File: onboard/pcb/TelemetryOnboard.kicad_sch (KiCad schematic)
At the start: 140 parts, among them J1 USB-C, J2 USB-C, J3 RFPC-SMA28-F, J4 RFPC-SMA28-F, M1 M4 Mounting Hole, M2 M4 Mounting Hole, M3 M4 Mounting Hole, M4 M4 Mounting Hole, Q1 NPN, U1 CP2102N, U2 CP2102N, U3 RC1780HP-RC232, U4 RC1701HP-RC232, U5 AVR128DB64x-xPT, U6 W25Q80DVSSIG

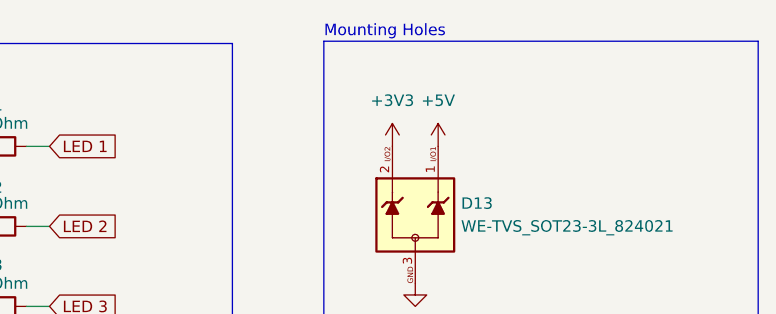
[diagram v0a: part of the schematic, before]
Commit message: change esd prot name
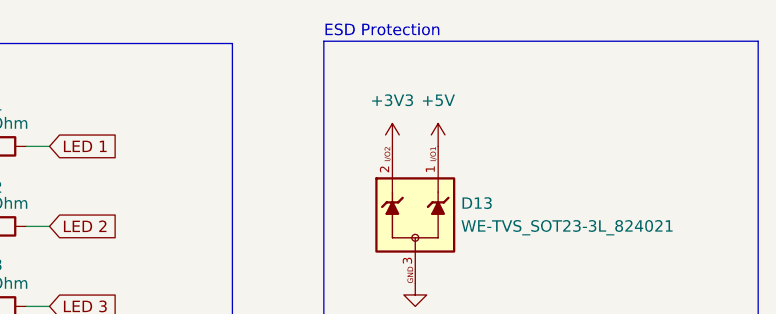
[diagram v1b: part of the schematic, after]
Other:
- note added: "ESD Protection"
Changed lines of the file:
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@@
 		)
 	)
-	(text "Mounting Holes"
+	(text "ESD Protection"
 		(exclude_from_sim no)
 		(at 520.7 24.13 0)

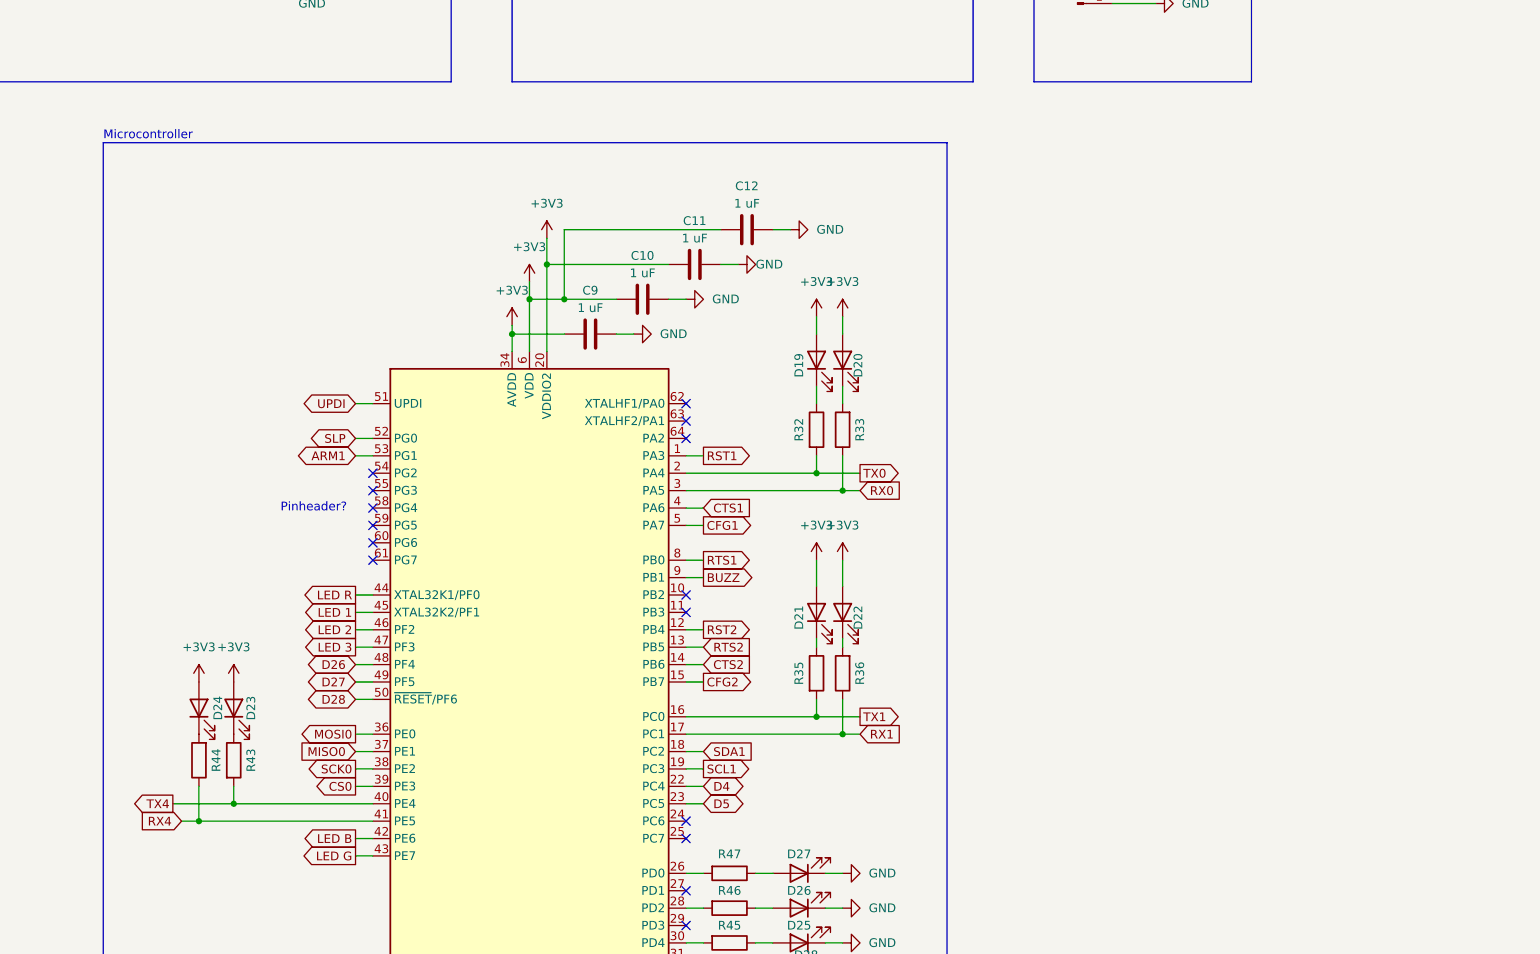
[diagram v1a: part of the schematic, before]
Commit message: add connector to umbilical connector
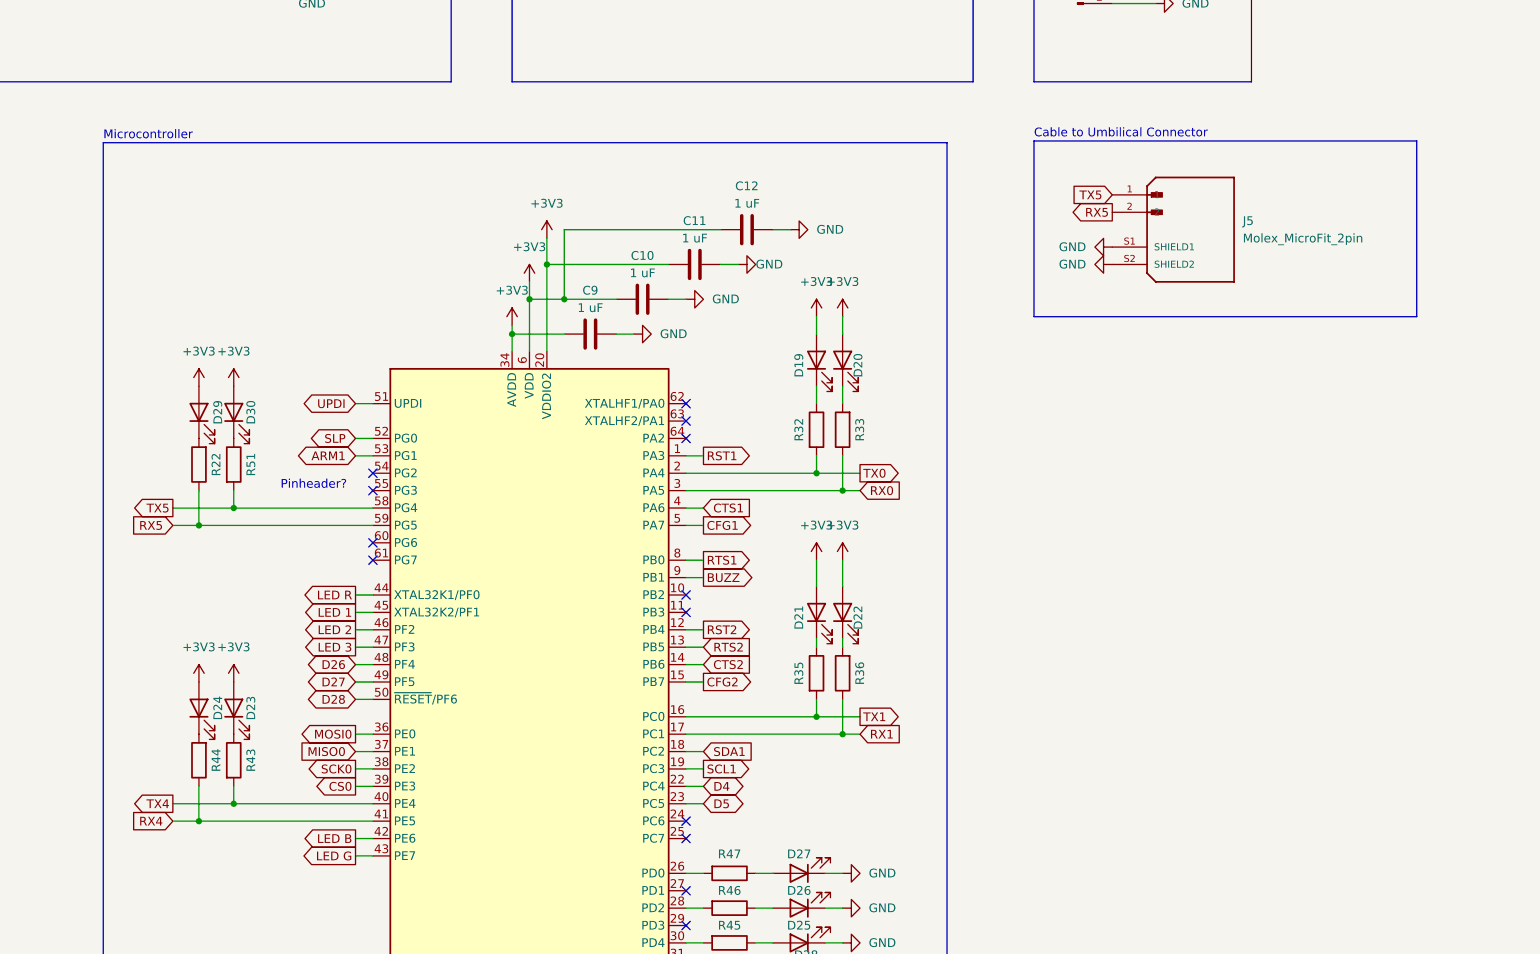
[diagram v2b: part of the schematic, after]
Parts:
- added D29, D30: red, LED_SMD:LED_0805_2012Metric_Pad1.15x1.40mm_HandSolder, symbol Device:LED
- added J5: Molex_MicroFit_2pin, Footprints:Molex_MicroFit_2pin, symbol Symbols:Molex_MicroFit_2pin
- added R22, R51: 1k, Resistor_SMD:R_0805_2012Metric_Pad1.20x1.40mm_HandSolder, symbol Device:R
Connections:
- net +3V3: now also D29.2 (A), D30.2 (A)
- net GND: now also J5.S1 (SHIELD1), J5.S2 (SHIELD2)
- net TX5: now reaches U5.58 (PG4)
- net TX5: now also J5.1, R51.2
- net RX5: now reaches U5.59 (PG5)
- net RX5: now also J5.2, R22.1
- new net: D29.1 (K), R22.2
- new net: D30.1 (K), R51.1
- no-connect marks 41 -> 39
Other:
- note added: "Cable to Umbilical Connector"

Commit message: place other components on pcb
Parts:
- removed D29, D30: red, LED_SMD:LED_0805_2012Metric_Pad1.15x1.40mm_HandSolder, symbol Device:LED
- removed R22, R51: 1k, Resistor_SMD:R_0805_2012Metric_Pad1.20x1.40mm_HandSolder, symbol Device:R
- removed TP9: TestPoint, Footprints:Test Point, symbol Connector:TestPoint
- added D21, D22: red, LED_SMD:LED_0805_2012Metric_Pad1.15x1.40mm_HandSolder, symbol Device:LED
- added R35, R36: 1k, Resistor_SMD:R_0805_2012Metric_Pad1.20x1.40mm_HandSolder, symbol Device:R
- TP36, TP37, TP38, TP39: now not fitted
- renumbered D21 to D29, D22 to D30, R35 to R22, R36 to R51
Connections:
- net +3V3: now also D21.2 (A), D22.2 (A)
- net BUZZ: now also U5.8 (PB0); no longer U5.9 (PB1)
- net CFG1: now also U5.3 (PA5); no longer U5.5 (PA7)
- net CFG2: now also U5.11 (PB3); no longer U5.15 (PB7)
- net CTS1: now also TP8.1, U5.1 (PA3); no longer TP4.1, U5.4 (PA6)
- net CTS2: now also TP13.1, U5.9 (PB1); no longer TP14.1, U5.14 (PB6)
- net D4: now also U5.24 (PC6); no longer U5.22 (PC4)
- net D5: now also U5.25 (PC7); no longer U5.23 (PC5)
- net LED 1: now also U5.47 (PF3); no longer U5.45 (XTAL32K2/PF1)
- net LED 3: now also U5.45 (XTAL32K2/PF1); no longer U5.47 (PF3)
- net RST1: now also U5.61 (PG7); no longer U5.1 (PA3)
- net RST2: now also U5.60 (PG6); no longer U5.12 (PB4)
- net RTS1: now also TP4.1, U5.2 (PA4); no longer TP8.1, U5.8 (PB0)
- net RTS2: now also TP14.1, U5.10 (PB2); no longer TP13.1, U5.13 (PB5)
- net RX0: now also U5.63 (XTALHF2/PA1); no longer U5.3 (PA5)
- net RX1: now also J5.1; no longer TP17.1, U4.5 (TXD)
- net TX0: now also U5.62 (XTALHF1/PA0); no longer U5.2 (PA4)
- net TX1: now also J5.2; no longer R37.1, TP16.1, U4.6 (RXD)
- net at R47.2: now also U5.15 (PB7); no longer U5.26 (PD0)
- net at R46.2: now also U5.14 (PB6); no longer U5.28 (PD2)
- net RX5: no longer names the net of U5.59 (PG5)
- net RX5: no longer J5.2
- net TX5: no longer names the net of U5.58 (PG4)
- net TX5: no longer J5.1
- new net: D22.1 (K), R36.2
- new net: D21.1 (K), R35.1
- new net RX3: R36.1, TP17.1, U4.5 (TXD), U5.13 (PB5)
- new net TX3: R35.2, R37.1, TP16.1, U4.6 (RXD), U5.12 (PB4)
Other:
- moved on the sheet: D19, D20, D26, D27, D29, D30, J5, R22, R32, R33, R46, R47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

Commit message: improve pcb layout
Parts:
- removed D23, D24: red, LED_SMD:LED_0805_2012Metric_Pad1.15x1.40mm_HandSolder, symbol Device:LED
- removed D28: orange, LED_SMD:LED_0805_2012Metric_Pad1.15x1.40mm_HandSolder, symbol Device:LED
- removed R43, R44: 1k, Resistor_SMD:R_0805_2012Metric_Pad1.20x1.40mm_HandSolder, symbol Device:R
- removed R48: 270R, Resistor_SMD:R_0805_2012Metric_Pad1.20x1.40mm_HandSolder, symbol Device:R
- renumbered D26 to D25, D27 to D26, D25 to D27, R46 to R45, R47 to R46, R45 to R47
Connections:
- net at U5.30 (PD4): no longer R47.2
- net at U5.33 (VREFA/PD7): now also R47.2
- no-connect marks 39 -> 40
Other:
- moved on the sheet: D27, R47

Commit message: small change
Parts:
- D11, D12, R20, R21: now fitted
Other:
- moved on the sheet: J5
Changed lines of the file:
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@@
 	)
 	(rectangle
-		(start 509.27 141.986)
-		(end 565.15 167.64)
+		(start 497.84 143.256)
+		(end 553.72 168.91)
 		(stroke
 			(width 0)
@@
 	(text "Cable to Umbilical Connector"
 		(exclude_from_sim no)
-		(at 509.27 140.97 0)
+		(at 497.84 142.24 0)
 		(effects
 			(font
@@
 	(global_label "TX1"
 		(shape input)
-		(at 520.7 152.4 180)
+		(at 509.27 153.67 180)
 		(fields_autoplaced yes)
 		(effects
@@
 		)
 		(property "Intersheetrefs" "${INTERSHEET_REFS}"
-			(at 514.3282 152.4 0)
+			(at 502.8982 153.67 0)
 			(effects
 				(font
@@
 	(global_label "RX1"
 		(shape output)
-		(at 520.7 149.86 180)
+		(at 509.27 151.13 180)
 		(fields_autoplaced yes)
 		(effects
@@
 		)
 		(property "Intersheetrefs" "${INTERSHEET_REFS}"
-			(at 514.0258 149.86 0)
+			(at 502.5958 151.13 0)
 			(effects
 				(font
@@
 	(symbol
 		(lib_id "power:GND")
-		(at 520.7 157.48 270)
+		(at 509.27 158.75 270)
 		(unit 1)
 		(exclude_from_sim no)
@@
 		(fields_autoplaced yes)
 		(property "Reference" "#PWR0111"
-			(at 514.35 157.48 0)
+			(at 502.92 158.75 0)
 			(effects
 				(font
@@
 		)
 		(property "Value" "GND"
-			(at 516.89 157.4799 90)
+			(at 505.46 158.7499 90)
 			(effects
 				(font
@@
 		)
 		(property "Footprint" ""
-			(at 520.7 157.48 0)
+			(at 509.27 158.75 0)
 			(effects
 				(font
@@
 		)
 		(property "Datasheet" ""
-			(at 520.7 157.48 0)
+			(at 509.27 158.75 0)
 			(effects
 				(font
@@
 		)
 		(property "Description" "Power symbol creates a global label with name \"GND\" , ground"
-			(at 520.7 157.48 0)
+			(at 509.27 158.75 0)
 			(effects
 				(font
@@
 	(symbol
 		(lib_id "Symbols:Molex_MicroFit_2pin")
-		(at 525.78 154.94 0)
+		(at 514.35 156.21 0)
 		(unit 1)
 		(exclude_from_sim no)
@@
 		(fields_autoplaced yes)
 		(property "Reference" "J5"
-			(at 539.75 153.6699 0)
+			(at 528.32 154.9399 0)
 			(effects
 				(font
@@
 		)
 		(property "Value" "Molex_MicroFit_2pin"
-			(at 539.75 156.2099 0)
+			(at 528.32 157.4799 0)
 			(effects
 				(font
@@
 		)
 		(property "Footprint" "Footprints:Molex_MicroFit_2pin"
-			(at 525.78 154.94 0)
+			(at 514.35 156.21 0)
 			(effects
 				(font
@@
 		)
 		(property "Datasheet" ""
-			(at 525.78 154.94 0)
+			(at 514.35 156.21 0)
 			(effects
 				(font
@@
 		)
 		(property "Description" ""
-			(at 525.78 154.94 0)
+			(at 514.35 156.21 0)
 			(effects
 				(font
@@
 		)
 		(property "DigiKey_Part_Number" "WM1870-ND"
-			(at 525.78 154.94 0)
+			(at 514.35 156.21 0)
 			(effects
 				(font
@@
 		)
 		(property "SnapEDA_Link" "https://www.snapeda.com/parts/436500203/Molex/view-part/?ref=snap"
-			(at 525.78 154.94 0)
+			(at 514.35 156.21 0)
 			(effects
 				(font
@@
 		)
 		(property "MAXIMUM_PACKAGE_HEIGHT" "5.57 mm"
-			(at 525.78 154.94 0)
+			(at 514.35 156.21 0)
 			(effects
 				(font
@@
 		)
 		(property "Package" "None"
-			(at 525.78 154.94 0)
+			(at 514.35 156.21 0)
 			(effects
 				(font
@@
 		)
 		(property "Check_prices" "https://www.snapeda.com/parts/436500203/Molex/view-part/?ref=eda"
-			(at 525.78 154.94 0)
+			(at 514.35 156.21 0)
 			(effects
 				(font
@@
 		)
 		(property "STANDARD" "Manufacturer Recommendations"
-			(at 525.78 154.94 0)
+			(at 514.35 156.21 0)
 			(effects
 				(font
@@
 		)
 		(property "PARTREV" "F3"
-			(at 525.78 154.94 0)
+			(at 514.35 156.21 0)
 			(effects
 				(font
@@
 		)
 		(property "MF" "Molex"
-			(at 525.78 154.94 0)
+			(at 514.35 156.21 0)
 			(effects
 				(font
@@
 		)
 		(property "MP" "436500203"
-			(at 525.78 154.94 0)
+			(at 514.35 156.21 0)
 			(effects
 				(font
@@
 		)
 		(property "Description_1" "Conn Wire to Board HDR 2 POS 3mm Solder RA Side Entry Thru-Hole Micro-Fit 3.0™ Tray"
-			(at 525.78 154.94 0)
+			(at 514.35 156.21 0)
 			(effects
 				(font
@@
 		)
 		(property "MANUFACTURER" "Molex"
-			(at 525.78 154.94 0)
+			(at 514.35 156.21 0)
 			(effects
 				(font
@@
 		(in_bom yes)
 		(on_board yes)
-		(dnp yes)
+		(dnp no)
 		(property "Reference" "D11"
 			(at 396.24 99.822 0)
@@
 		(in_bom yes)
 		(on_board yes)
-		(dnp yes)
+		(dnp no)
 		(property "Reference" "R20"
 			(at 406.4 99.568 90)
@@
 		(in_bom yes)
 		(on_board yes)
-		(dnp yes)
+		(dnp no)
 		(property "Reference" "D12"
 			(at 396.24 109.982 0)
@@
 	(symbol
 		(lib_id "power:GND")
-		(at 520.7 160.02 270)
+		(at 509.27 161.29 270)
 		(unit 1)
 		(exclude_from_sim no)
@@
 		(fields_autoplaced yes)
 		(property "Reference" "#PWR0112"
-			(at 514.35 160.02 0)
+			(at 502.92 161.29 0)
 			(effects
 				(font
@@
 		)
 		(property "Value" "GND"
-			(at 516.89 160.0199 90)
+			(at 505.46 161.2899 90)
 			(effects
 				(font
@@
 		)
 		(property "Footprint" ""
-			(at 520.7 160.02 0)
+			(at 509.27 161.29 0)
 			(effects
 				(font
@@
 		)
 		(property "Datasheet" ""
-			(at 520.7 160.02 0)
+			(at 509.27 161.29 0)
 			(effects
 				(font
@@
 		)
 		(property "Description" "Power symbol creates a global label with name \"GND\" , ground"
-			(at 520.7 160.02 0)
+			(at 509.27 161.29 0)
 			(effects
 				(font
@@
 		(in_bom yes)
 		(on_board yes)
-		(dnp yes)
+		(dnp no)
 		(property "Reference" "R21"
 			(at 406.4 109.728 90)
